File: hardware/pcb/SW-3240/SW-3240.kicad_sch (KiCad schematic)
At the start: 47 parts, among them J1 AUX_MIC_IN, J10 FP_IO, J11 RESET/FLASH, J12 PWR, J13 BAT, J14 CH_1, J15 CH_2, J16 CH_3, J17 CH_4, J2 AUX_LINE_IN, J3 MIC, J4 LINE IN, J5 JTAG, J6 ESPFlash, J8 I2C, J9 MIC_IN_R, U1 SW-32MA, U2 MCP4728, U3 ESP32-WROOM-32D, U4 Channel 1, U5 Channel 2, U6 Channel 3, U7 Channel 4

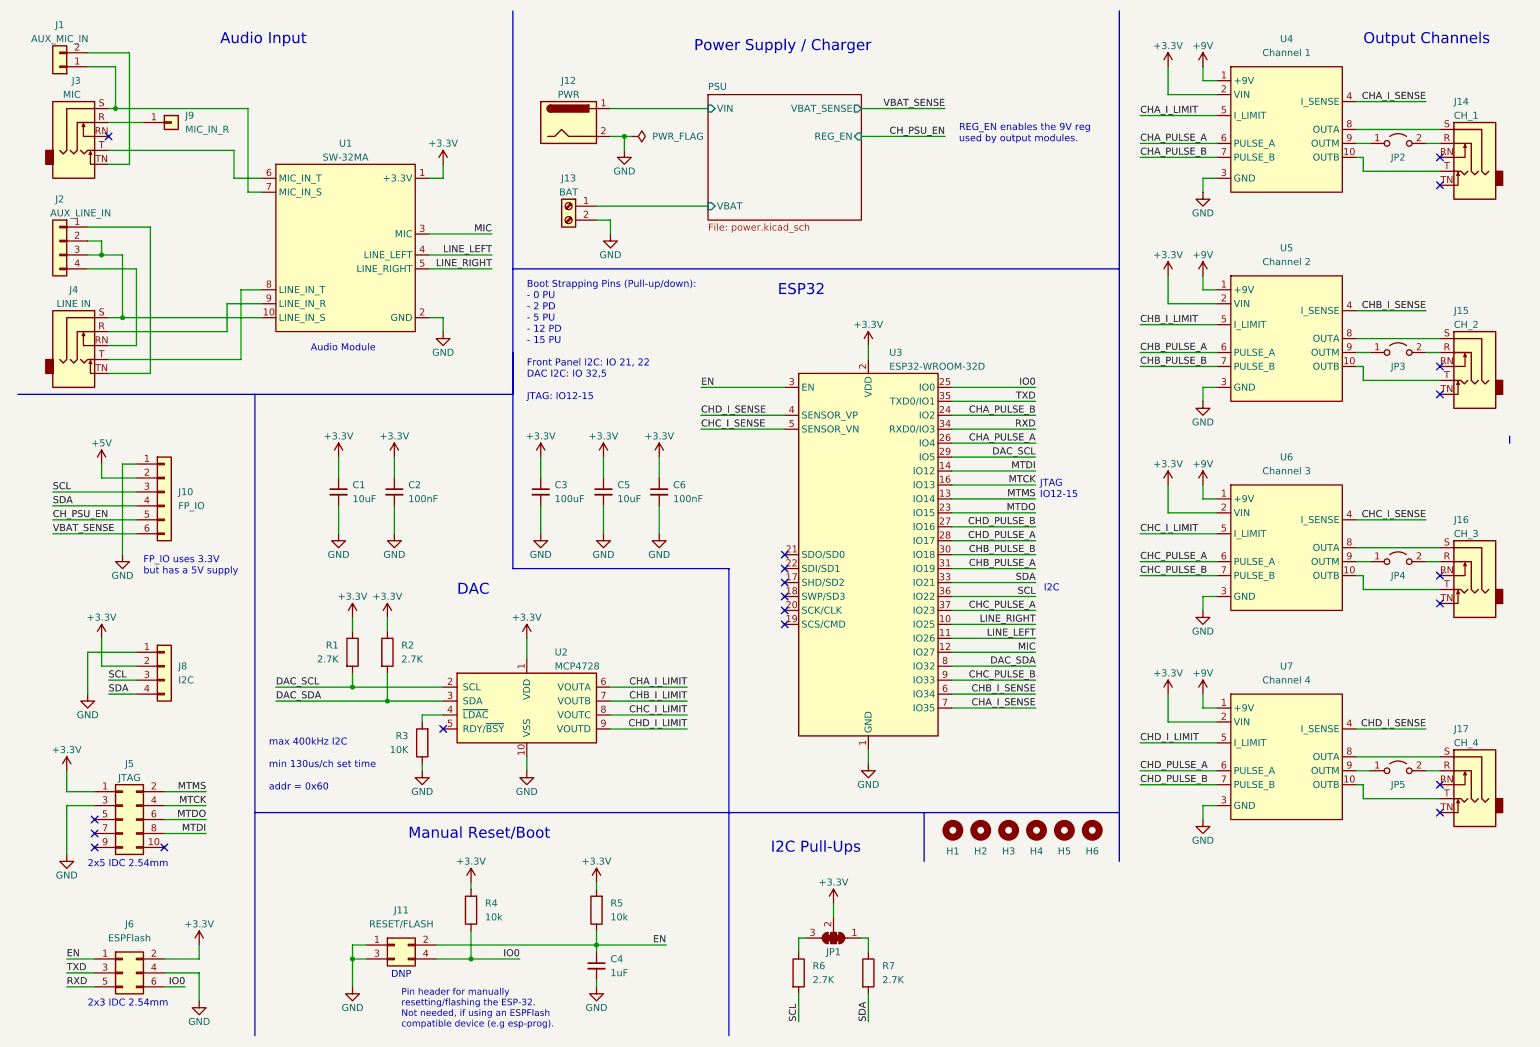
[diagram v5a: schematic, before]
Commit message: use atmega328pb for main board
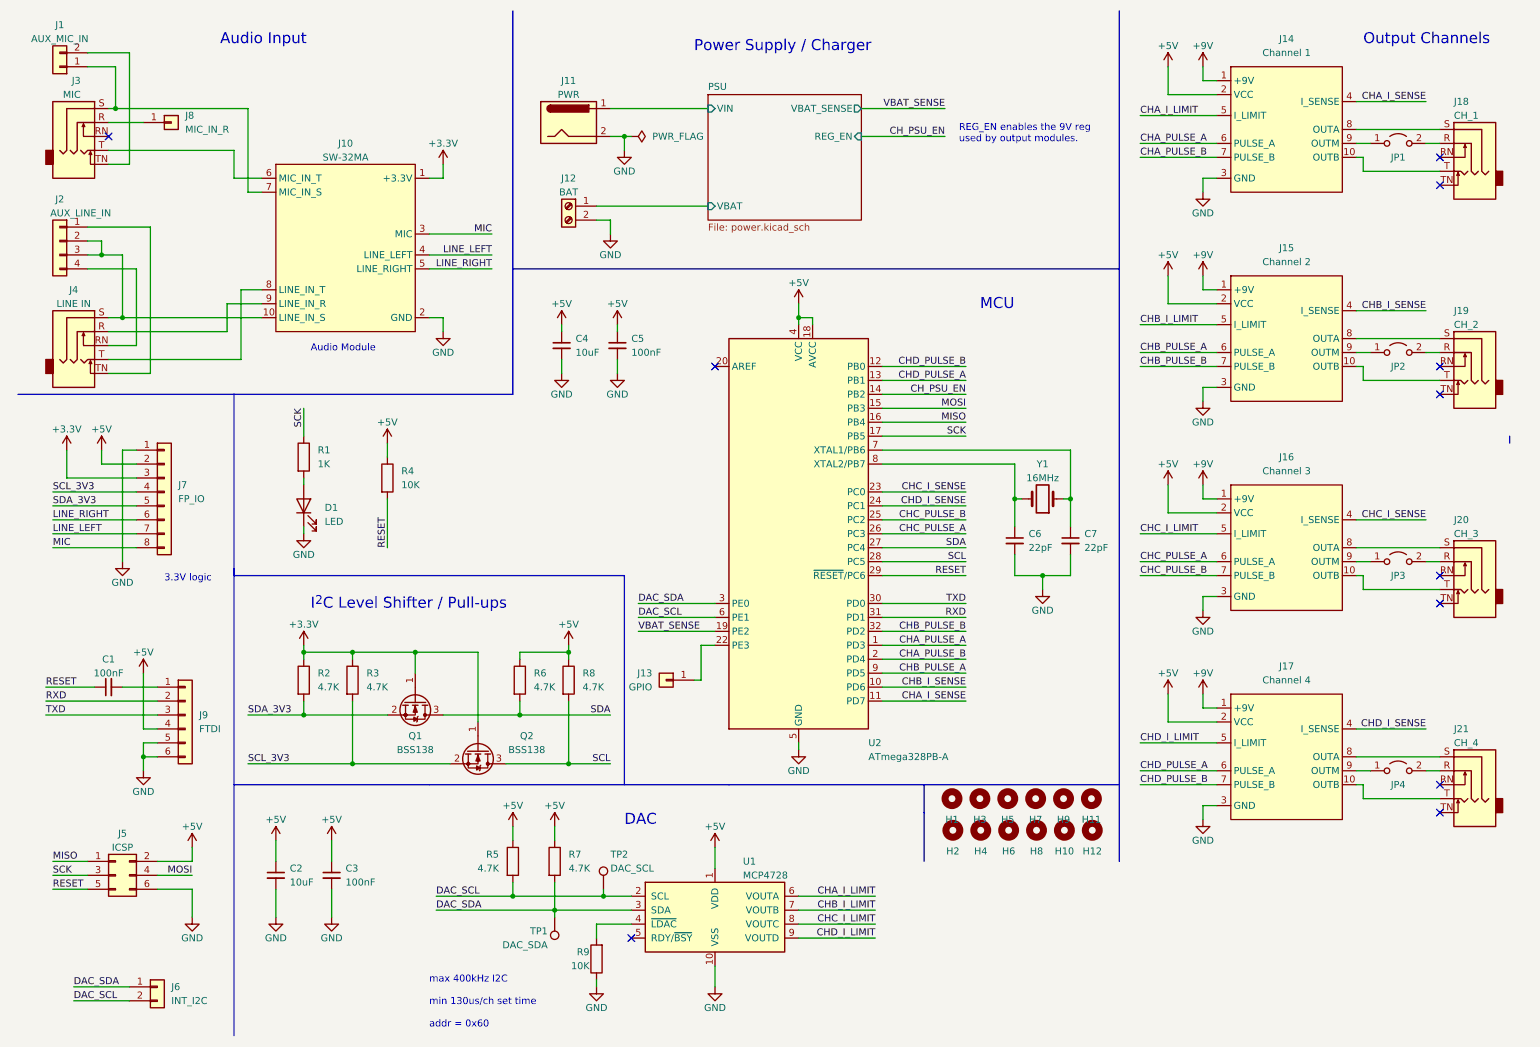
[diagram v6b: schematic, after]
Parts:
- removed C3: 100uF, Capacitor_SMD:C_0603_1608Metric, symbol Device:C_Small
- removed C4: 1uF, Capacitor_SMD:C_0603_1608Metric, symbol Device:C_Small
- removed J11: RESET/FLASH, Connector_PinHeader_2.54mm:PinHeader_2x02_P2.54mm_Vertical, symbol Connector_Generic:Conn_02x02_Odd_Even
- removed J5: JTAG, Connector_PinHeader_2.54mm:PinHeader_2x05_P2.54mm_Vertical, symbol Connector_Generic:Conn_02x05_Odd_Even
- removed J8: I2C, Connector_PinHeader_2.54mm:PinHeader_1x04_P2.54mm_Vertical, symbol Connector_Generic:Conn_01x04
- removed JP1: SolderJumper_3_Bridged123, SaawLib:SolderJumper-3_P1.3mm_Bridged123_Pad1.0x1.5mm_NumberLabels, symbol Jumper:SolderJumper_3_Bridged123
- removed R5: 10k, Resistor_SMD:R_0603_1608Metric, symbol Device:R
- removed R7: 2.7K, Resistor_SMD:R_0603_1608Metric, symbol Device:R
- removed U3: ESP32-WROOM-32D, RF_Module:ESP32-WROOM-32, symbol RF_Module:ESP32-WROOM-32D
- added C1: 100nF, Capacitor_SMD:C_0603_1608Metric, symbol Device:C_Small
- added C6, C7: 22pF, Capacitor_SMD:C_0603_1608Metric, symbol Device:C_Small
- added D1: LED, LED_SMD:LED_0603_1608Metric, symbol Device:LED
- added H1, H11, H3, H5, H7, H9: MountingHole, MountingHole:MountingHole_2.2mm_M2, symbol Mechanical:MountingHole
- added J13: GPIO, Connector_PinHeader_2.54mm:PinHeader_1x01_P2.54mm_Vertical, symbol Connector_Generic:Conn_01x01
- added J6: INT_I2C, Connector_PinHeader_2.54mm:PinHeader_1x02_P2.54mm_Vertical, symbol Connector_Generic:Conn_01x02
- added J9: FTDI, Connector_PinHeader_2.54mm:PinHeader_1x06_P2.54mm_Vertical, symbol Connector_Generic:Conn_01x06
- added Q1, Q2: BSS138, Package_TO_SOT_SMD:SOT-23, symbol Transistor_FET:BSS138
- added R1: 1K, Resistor_SMD:R_0603_1608Metric, symbol Device:R
- added R2, R3, R8: 4.7K, Resistor_SMD:R_0603_1608Metric, symbol Device:R
- added TP1: DAC_SDA, TestPoint:TestPoint_THTPad_D2.0mm_Drill1.0mm, symbol Connector:TestPoint
- added TP2: DAC_SCL, TestPoint:TestPoint_THTPad_D2.0mm_Drill1.0mm, symbol Connector:TestPoint
- added U2: ATmega328PB-A, Package_QFP:TQFP-32_7x7mm_P0.8mm, symbol MCU_Microchip_ATmega:ATmega328PB-A
- added Y1: 16MHz, Crystal:Crystal_HC49-4H_Vertical, symbol Device:Crystal
- J10: renamed from U1; now left out of the parts list
- J11: renamed from J12; MOUSER (none) -> 490-PJ-102AH; MPN (none) -> PJ-102AH
- J14: renamed from U4; now left out of the parts list
- J15: renamed from U5; now left out of the parts list
- J16: renamed from U6; now left out of the parts list
- J17: renamed from U7; now left out of the parts list
- J18: renamed from J14; MOUSER (none) -> 806-STX-3100-5N; MPN (none) -> STX-3100-5N
- J19: renamed from J15; MOUSER (none) -> 806-STX-3100-5N; MPN (none) -> STX-3100-5N
- J20: renamed from J16; MOUSER (none) -> 806-STX-3100-5N; MPN (none) -> STX-3100-5N
- J21: renamed from J17; MOUSER (none) -> 806-STX-3100-5N; MPN (none) -> STX-3100-5N
- J5: renamed from J6; value ESPFlash -> ICSP
- J7: renamed from J10; footprint Connector_JST:JST_XH_B6B-XH-A_1x06_P2.50mm_Vertical -> Connector_JST:JST_XH_B7B-XH-A_1x07_P2.50mm_Vertical; symbol Connector_Generic:Conn_01x06 -> Connector_Generic:Conn_01x08
- J8: renamed from J9; now left out of the parts list
- R4: value 10k -> 10K
- R5: renamed from R1; value 2.7K -> 4.7K
- R6: value 2.7K -> 4.7K
- R7: renamed from R2; value 2.7K -> 4.7K
- U1: renamed from U2; LCSC (none) -> C108207; MOUSER (none) -> 579-MCP4728-E/UN; MPN (none) -> MCP4728-E/UN
- renumbered C1 to C2, C2 to C3, C5 to C4, C6 to C5, H5 to H10, H6 to H12, H1 to H2, H2 to H4, H3 to H6, H4 to H8, J13 to J12, JP2 to JP1, JP3 to JP2, JP4 to JP3, JP5 to JP4, R3 to R9
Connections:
- net +3V3: now also J7.3 (Pin_3), Q1.1 (G), Q2.1 (G), R2.1, R3.1; no longer C2.1, C3.1, C4.1, C5.1, J14.2 (VIN), J15.2 (VIN), J16.2 (VIN), J17.2 (VIN), J5.2 (Pin_2), R4.2, R5.1, R7.1, U1.1 (VDD)
- net +5V: now also C2.1, C3.1, C4.1, C5.1, J14.2 (VCC), J15.2 (VCC), J16.2 (VCC), J17.2 (VCC), J5.2 (Pin_2), R4.1, R5.1, R6.1, R7.1, U1.1 (VDD), J9.4 (Pin_4), R8.1, U2.18 (AVCC), U2.4 (VCC)
- net CHA_I_SENSE: now also U2.11 (PD7)
- net CHA_PULSE_A: now also U2.1 (PD3)
- net CHA_PULSE_B: now also U2.2 (PD4)
- net CHB_I_SENSE: now also U2.10 (PD6)
- net CHB_PULSE_A: now also U2.9 (PD5)
- net CHB_PULSE_B: now also U2.32 (PD2)
- net CHC_I_SENSE: now also U2.23 (PC0)
- net CHC_PULSE_A: now also U2.26 (PC3)
- net CHC_PULSE_B: now also U2.25 (PC2)
- net CHD_I_SENSE: now also U2.24 (PC1)
- net CHD_PULSE_A: now also U2.13 (PB1)
- net CHD_PULSE_B: now also U2.12 (PB0)
- net CH_PSU_EN: now also U2.14 (PB2); no longer J7.5 (Pin_5)
- net DAC_SCL: now also J6.2 (Pin_2), TP2.1, U2.6 (PE1)
- net DAC_SDA: now also J6.1 (Pin_1), TP1.1, U2.3 (PE0)
- net GND: now also J5.6 (Pin_6), C6.2, C7.2, D1.1 (K), J9.5 (Pin_5), J9.6 (Pin_6), U2.21 (GND), U2.5 (GND); no longer J5.4 (Pin_4)
- net LINE_LEFT: now also J7.7 (Pin_7)
- net LINE_RIGHT: now also J7.6 (Pin_6)
- net MIC: now also J7.8 (Pin_8)
- net RXD: now also J9.2 (Pin_2), U2.31 (PD1); no longer J5.5 (Pin_5)
- net SCL: now also Q2.3 (D), R8.2, U2.28 (PC5); no longer J7.3 (Pin_3), R6.2
- net SDA: now also R6.2, Q1.3 (D), U2.27 (PC4); no longer J7.4 (Pin_4)
- net TXD: now also J9.3 (Pin_3), U2.30 (PD0); no longer J5.3 (Pin_3)
- net VBAT_SENSE: now also U2.19 (PE2); no longer J7.6 (Pin_6)
- net EN renamed MISO
- net MISO: now also U2.16 (PB4)
- removed net IO0: J5.6 (Pin_6), R4.1
- new net: C1.2, J9.1 (Pin_1)
- new net: C7.1, U2.7 (XTAL1/PB6), Y1.1
- new net: C6.1, U2.8 (XTAL2/PB7), Y1.2
- new net: J13.1 (Pin_1), U2.22 (PE3)
- new net: D1.2 (A), R1.2
- new net MOSI: J5.4 (Pin_4), U2.15 (PB3)
- new net RESET: C1.1, J5.5 (Pin_5), R4.2, U2.29 (~{RESET}/PC6)
- new net SCK: J5.3 (Pin_3), R1.1, U2.17 (PB5)
- new net SCL_3V3: J7.4 (Pin_4), Q2.2 (S), R3.2
- new net SDA_3V3: J7.5 (Pin_5), Q1.2 (S), R2.2
- no-connect marks 20 -> 11
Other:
- note added: "3.3V logic"
- note added: "I^{2}C Level Shifter / Pull-ups"
- note added: "MCU"
- note removed: "2x3 IDC 2.54mm"
- note removed: "2x5 IDC 2.54mm"
- note removed: "Boot Strapping Pins (Pull-up/down): - 0 PU - 2 PD - 5 PU - 12 PD - 15 PU Front Panel I2C: IO 21, 22 DAC I2C: IO 32,5 JTAG: IO12-15"
- note removed: "DNP"
- note removed: "ESP32"
- note removed: "FP_IO uses 3.3V but has a 5V supply"
- note removed: "I2C"
- note removed: "I2C Pull-Ups"
- note removed: "JTAG IO12-15"
- note removed: "Manual Reset/Boot"
- note removed: "Pin header for manually resetting/flashing the ESP-32. Not needed, if using an ESPFlash compatible device (e.g esp-prog)."
- moved on the sheet: C2, C3, C4, C5, J5, R5, R7, R9, U1

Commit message: major changes
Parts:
- removed J13: GPIO, Connector_PinHeader_2.54mm:PinHeader_1x01_P2.54mm_Vertical, symbol Connector_Generic:Conn_01x01
- removed J6: INT_I2C, Connector_PinHeader_2.54mm:PinHeader_1x02_P2.54mm_Vertical, symbol Connector_Generic:Conn_01x02
- removed TP1: DAC_SDA, TestPoint:TestPoint_THTPad_D2.0mm_Drill1.0mm, symbol Connector:TestPoint
- removed TP2: DAC_SCL, TestPoint:TestPoint_THTPad_D2.0mm_Drill1.0mm, symbol Connector:TestPoint
- C1, C3, C5: LCSC (none) -> C1591; MOUSER (none) -> 187-CL10B104KB8NNNC; MPN (none) -> CL10B104KB8NNNC
- C2, C4: LCSC (none) -> C2922482; MOUSER (none) -> 187-CL10A106MA8NRNC; MPN (none) -> CL10A106MA8NRNC
- D1: MOUSER (none) -> 710-150060VS75000; MPN (none) -> 150060VS75000
- H1, H10, H11, H12, H2, H3, H4, H5, H6, H7, H8, H9: now left out of the parts list
- J12: renamed from J14; now in the parts list
- J13: renamed from J15; now in the parts list
- J14: renamed from J16; now in the parts list
- J15: renamed from J17; now in the parts list
- J3, J4: MOUSER (none) -> 806-STX-3100-5N; MPN (none) -> STX-3100-5N
- J6: renamed from J7; footprint Connector_JST:JST_XH_B7B-XH-A_1x07_P2.50mm_Vertical -> Connector_JST:JST_XH_B8B-XH-A_1x08_P2.50mm_Vertical
- J9: renamed from J10; now in the parts list
- JP1: value TRI_PHASE -> JP1
- JP2: value TRI_PHASE -> JP2
- JP3: value TRI_PHASE -> JP3
- JP4: value TRI_PHASE -> JP4
- Q1, Q2: MPN (none) -> BSS138
- R1: LCSC (none) -> C22548; MOUSER (none) -> 603-RC0603FR-071KL; MPN (none) -> RC0603FR-071KL
- R2, R3, R5, R6, R7, R8: LCSC (none) -> C99782; MOUSER (none) -> 603-RC0603FR-074K7L; MPN (none) -> RC0603FR-074K7L
- R4, R9: LCSC (none) -> C98220; MOUSER (none) -> 603-RC0603FR-0710KL; MPN (none) -> RC0603FR-0710KL
- U2: value ATmega328PB-A -> ATmega328PB-AU; LCSC (none) -> C132230; MOUSER (none) -> 556-ATMEGA328PB-AU; MPN (none) -> ATMEGA328PB-AU
- renumbered J11 to J10, J12 to J11, J18 to J16, J19 to J17, J20 to J18, J21 to J19, J8 to J7, J9 to J8
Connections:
- net CHA_I_LIMIT renamed CHA_LEVEL
- net CHB_I_LIMIT renamed CHB_LEVEL
- net CHC_I_LIMIT renamed CHC_LEVEL
- net CHD_I_LIMIT renamed CHD_LEVEL
- no-connect marks 11 -> 12
